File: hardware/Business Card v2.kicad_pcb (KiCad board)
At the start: 2 copper layers, 85.4 x 54.1 mm, 39 parts, among them J1 Conn_01x03_Pin, Q1 DMP21D0UFB4-P, U1 ATTINY816-MNR, U3 NT3H2111W0FHKH

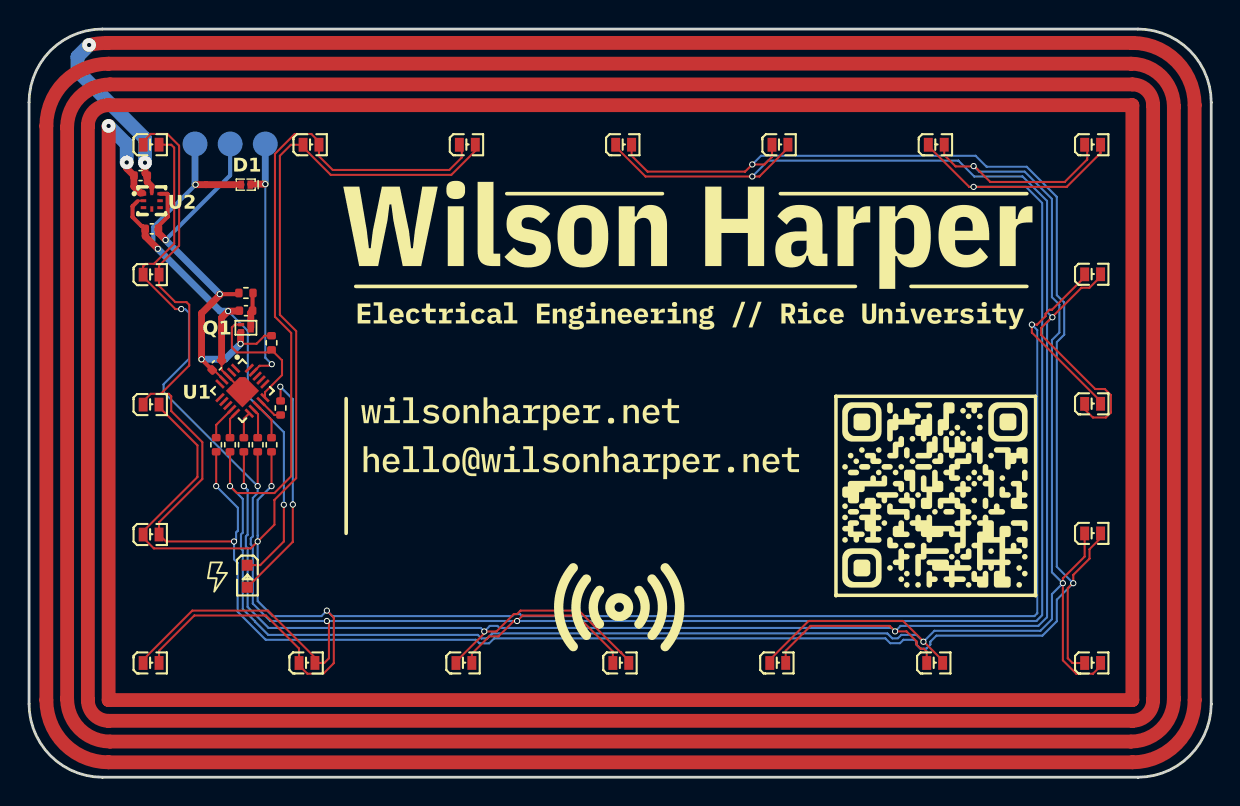
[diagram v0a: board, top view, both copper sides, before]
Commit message: 調布組込みラボ版 NFC 基板名刺
WiHarper/nfc_card（752793d）のフォーク。シルクを調布組込みラボ版に差し替え、
JLCPCB で部品実装まで発注できるよう BOM を修正した（C1 の LCSC 番号の
サイズ違いを修正、R4 に LCSC 番号を追加、JLCPCB 用の製造データを追加）。
回路・アンテナ・部品配置・配線は元の設計のまま。変更点は docs/CHANGES.md に記録。

Co-Authored-By: Claude Opus 5.5 <noreply@anthropic.com>
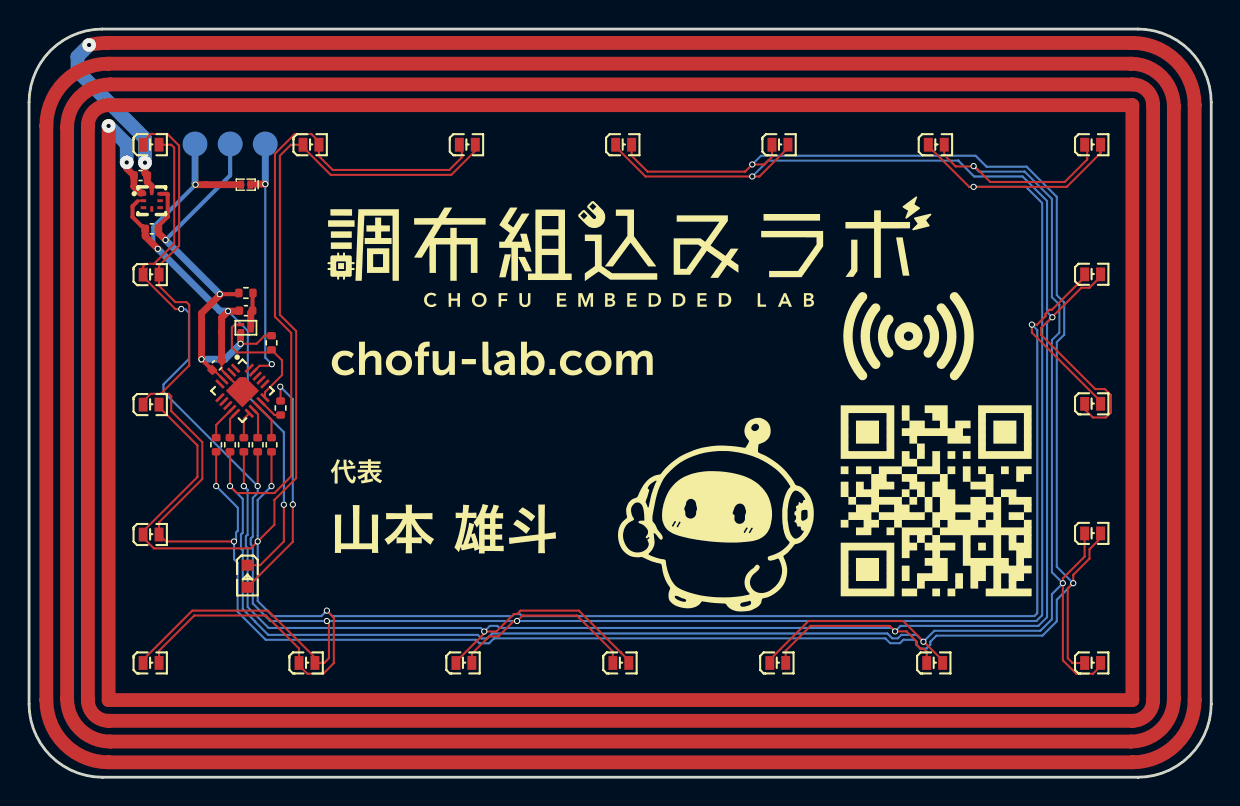
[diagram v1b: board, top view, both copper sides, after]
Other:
- board text removed: "Q1"
- board text removed: "U1"
- board text removed: "U2"
